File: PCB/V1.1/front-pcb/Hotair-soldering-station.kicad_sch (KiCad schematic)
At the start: 25 parts, among them J1 solder_select, J2 main-board-conn, J3 hot_on, J4 solder_on, SW1 HOTAIR_UP, SW2 HOTAIR_DOWN, SW3 SIRON_UP, SW4 SIRON_DOWN, SW5 SIRON_UP, SW6 SIRON_DOWN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

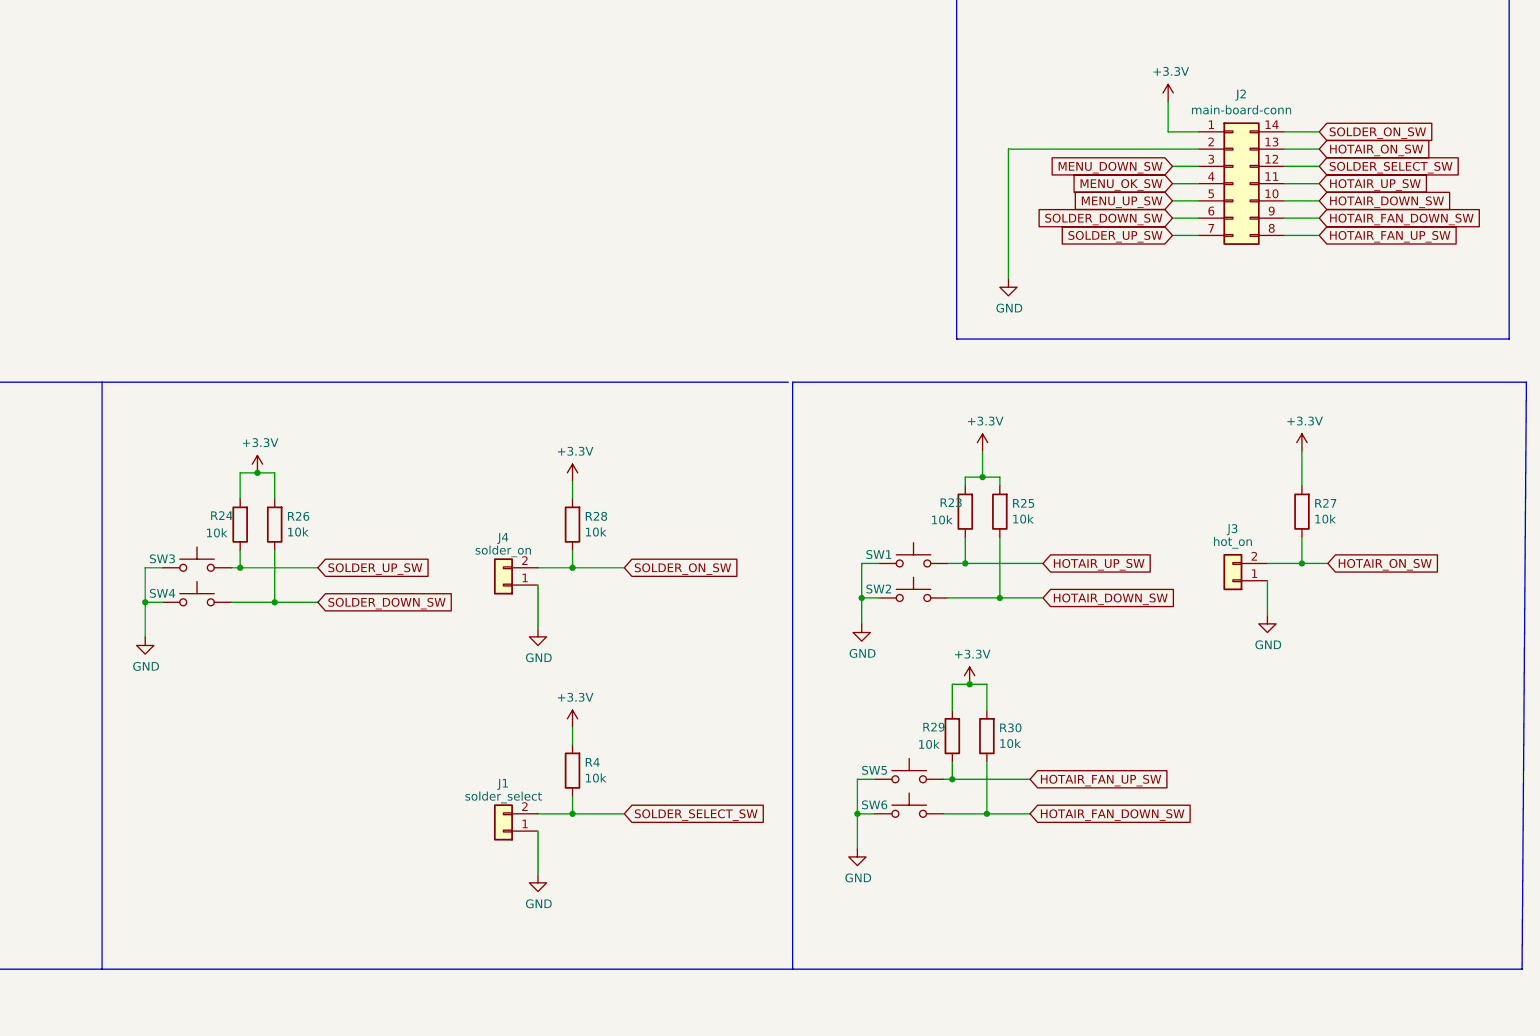
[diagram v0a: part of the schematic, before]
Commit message: Front Panel PCB design
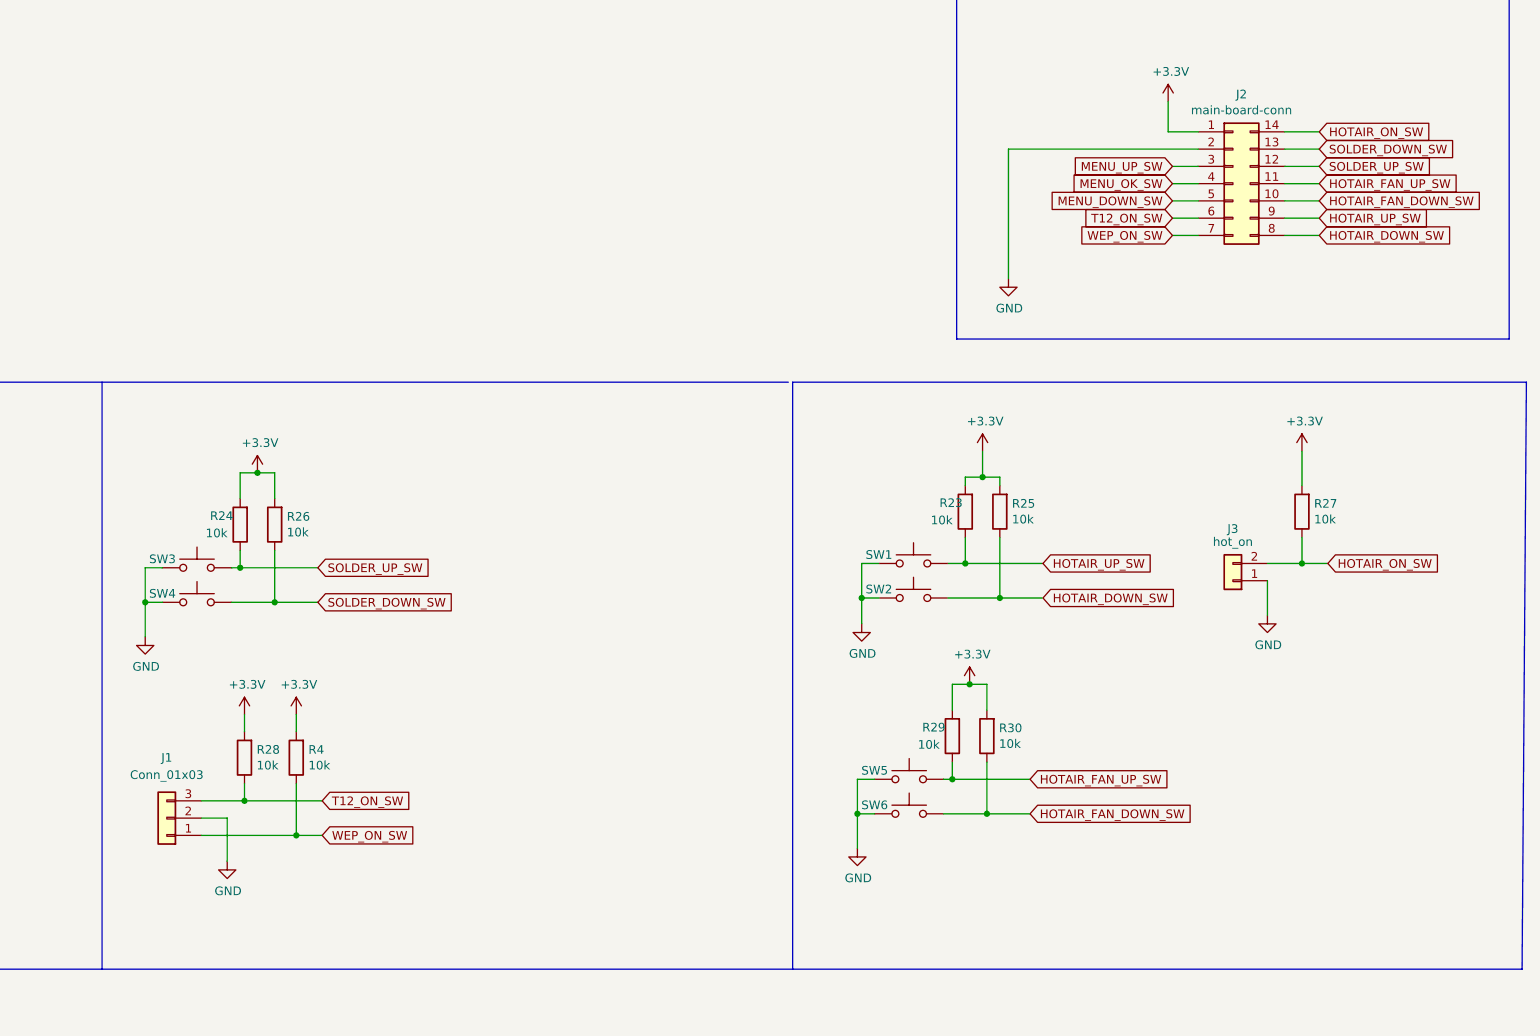
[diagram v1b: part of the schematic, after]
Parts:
- removed J1: solder_select, Connector_PinHeader_2.54mm:PinHeader_1x02_P2.54mm_Vertical, symbol Connector_Generic:Conn_01x02
- removed J4: solder_on, Connector_PinHeader_2.54mm:PinHeader_1x02_P2.54mm_Vertical, symbol Connector_Generic:Conn_01x02
- added J1: Conn_01x03, Connector_PinHeader_2.54mm:PinHeader_1x03_P2.54mm_Vertical, symbol Connector_Generic:Conn_01x03
- SW5: value SIRON_UP -> FAN_UP
- SW6: value SIRON_DOWN -> FAN_DOWN
- SW7: value SIRON_DOWN -> MENU_UP; footprint Switches:TACTILE_SWITCH_PTH_12MM -> My-Footprints:TACTILE_SWITCH_PTH_12MM
- SW8: value SIRON_UP -> MENU_DOWN; footprint Switches:TACTILE_SWITCH_PTH_12MM -> My-Footprints:TACTILE_SWITCH_PTH_12MM
- SW9: value SIRON_DOWN -> MENU_OK; footprint Switches:TACTILE_SWITCH_PTH_12MM -> My-Footprints:TACTILE_SWITCH_PTH_12MM
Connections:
- net GND: now also J1.2 (Pin_2)
- net HOTAIR_DOWN_SW: now also J2.8 (Pin_8); no longer J2.10 (Pin_10)
- net HOTAIR_FAN_DOWN_SW: now also J2.10 (Pin_10); no longer J2.9 (Pin_9)
- net HOTAIR_FAN_UP_SW: now also J2.11 (Pin_11); no longer J2.8 (Pin_8)
- net HOTAIR_ON_SW: now also J2.14 (Pin_14); no longer J2.13 (Pin_13)
- net HOTAIR_UP_SW: now also J2.9 (Pin_9); no longer J2.11 (Pin_11)
- net MENU_DOWN_SW: now also J2.5 (Pin_5); no longer J2.3 (Pin_3)
- net MENU_UP_SW: now also J2.3 (Pin_3); no longer J2.5 (Pin_5)
- net SOLDER_DOWN_SW: now also J2.13 (Pin_13); no longer J2.6 (Pin_6)
- net SOLDER_UP_SW: now also J2.12 (Pin_12); no longer J2.7 (Pin_7)
- net SOLDER_ON_SW renamed T12_ON_SW
- net T12_ON_SW: now also J2.6 (Pin_6), J1.3 (Pin_3); no longer J2.14 (Pin_14)
- net SOLDER_SELECT_SW renamed WEP_ON_SW
- net WEP_ON_SW: now also J2.7 (Pin_7), J1.1 (Pin_1); no longer J2.12 (Pin_12)
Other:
- moved on the sheet: R28, R4
